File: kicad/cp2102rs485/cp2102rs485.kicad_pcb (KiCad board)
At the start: 2 copper layers, 27.9 x 69.9 mm, 27 parts, among them J1 USB_B, J2 Conn_02x08_Counter_Clockwise, J3 Screw_Terminal_01x04, J4 Screw_Terminal_01x04, U1 TPD4E02B04DQA, U2 CP2102N-A01-GQFN28, U3 MAX485E

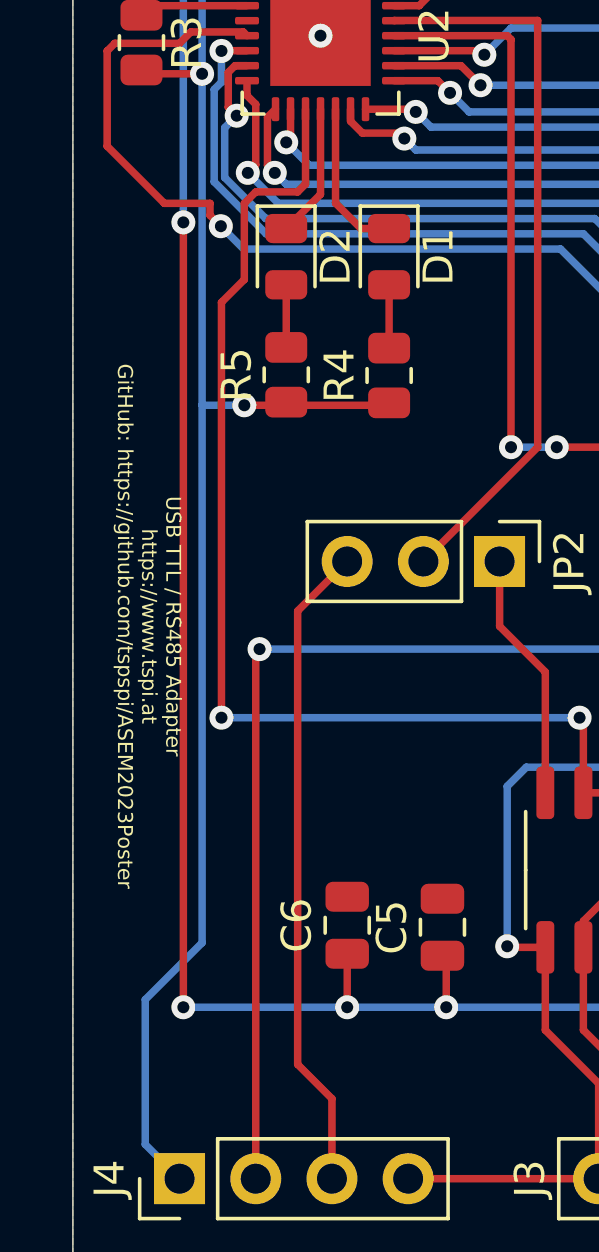
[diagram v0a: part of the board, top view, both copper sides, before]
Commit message: Update labeling to reflect commit number
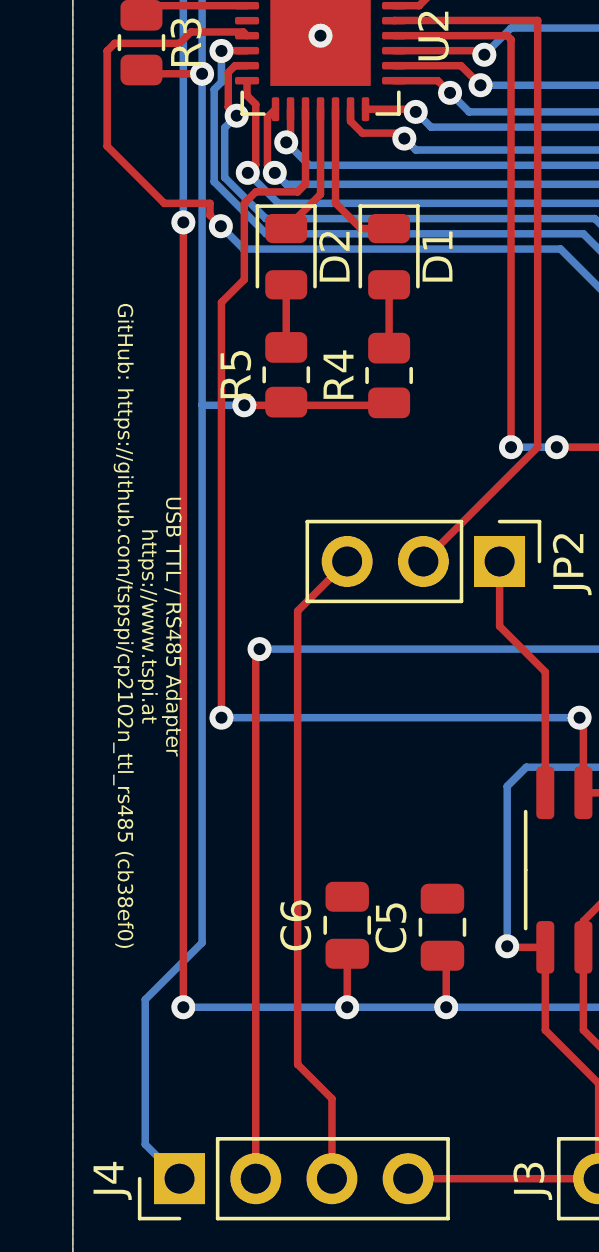
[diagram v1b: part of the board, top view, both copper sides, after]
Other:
- board text added: "USB TTL / RS485 Adapter https://www.tspi.at GitHub: https://github.com/tspspi/cp2102n_ttl_rs485 (cb38ef0)"
- board text removed: "USB TTL / RS485 Adapter https://www.tspi.at GitHub: https://github.com/tspspi/ASEM2023Poster"
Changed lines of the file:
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@@
     (46 B.CrtYd user)
     (47 F.CrtYd user)
-    (48 B.Fab user)
+    (48 B.Fab user hide)
     (49 F.Fab user)
   )
@@
     (effects (font (size 0.5 0.5) (thickness 0.075)) (justify left))
   )
-  (gr_text "USB TTL / RS485 Adapter\nhttps://www.tspi.at\nGitHub: https://github.com/tspspi/ASEM2023Poster" (at 83.82 73.66 270) (layer F.SilkS)
+  (gr_text "USB TTL / RS485 Adapter\nhttps://www.tspi.at\nGitHub: https://github.com/tspspi/cp2102n_ttl_rs485 (cb38ef0)" (at 83.82 73.66 -90) (layer F.SilkS)
     (effects (font (size 0.5 0.5) (thickness 0.075)))
   )
